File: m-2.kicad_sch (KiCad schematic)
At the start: 26 parts, among them J2 1-2199230-6, M3 M2_2280, Y1 ECS-327MVATX-2-CN-TR3

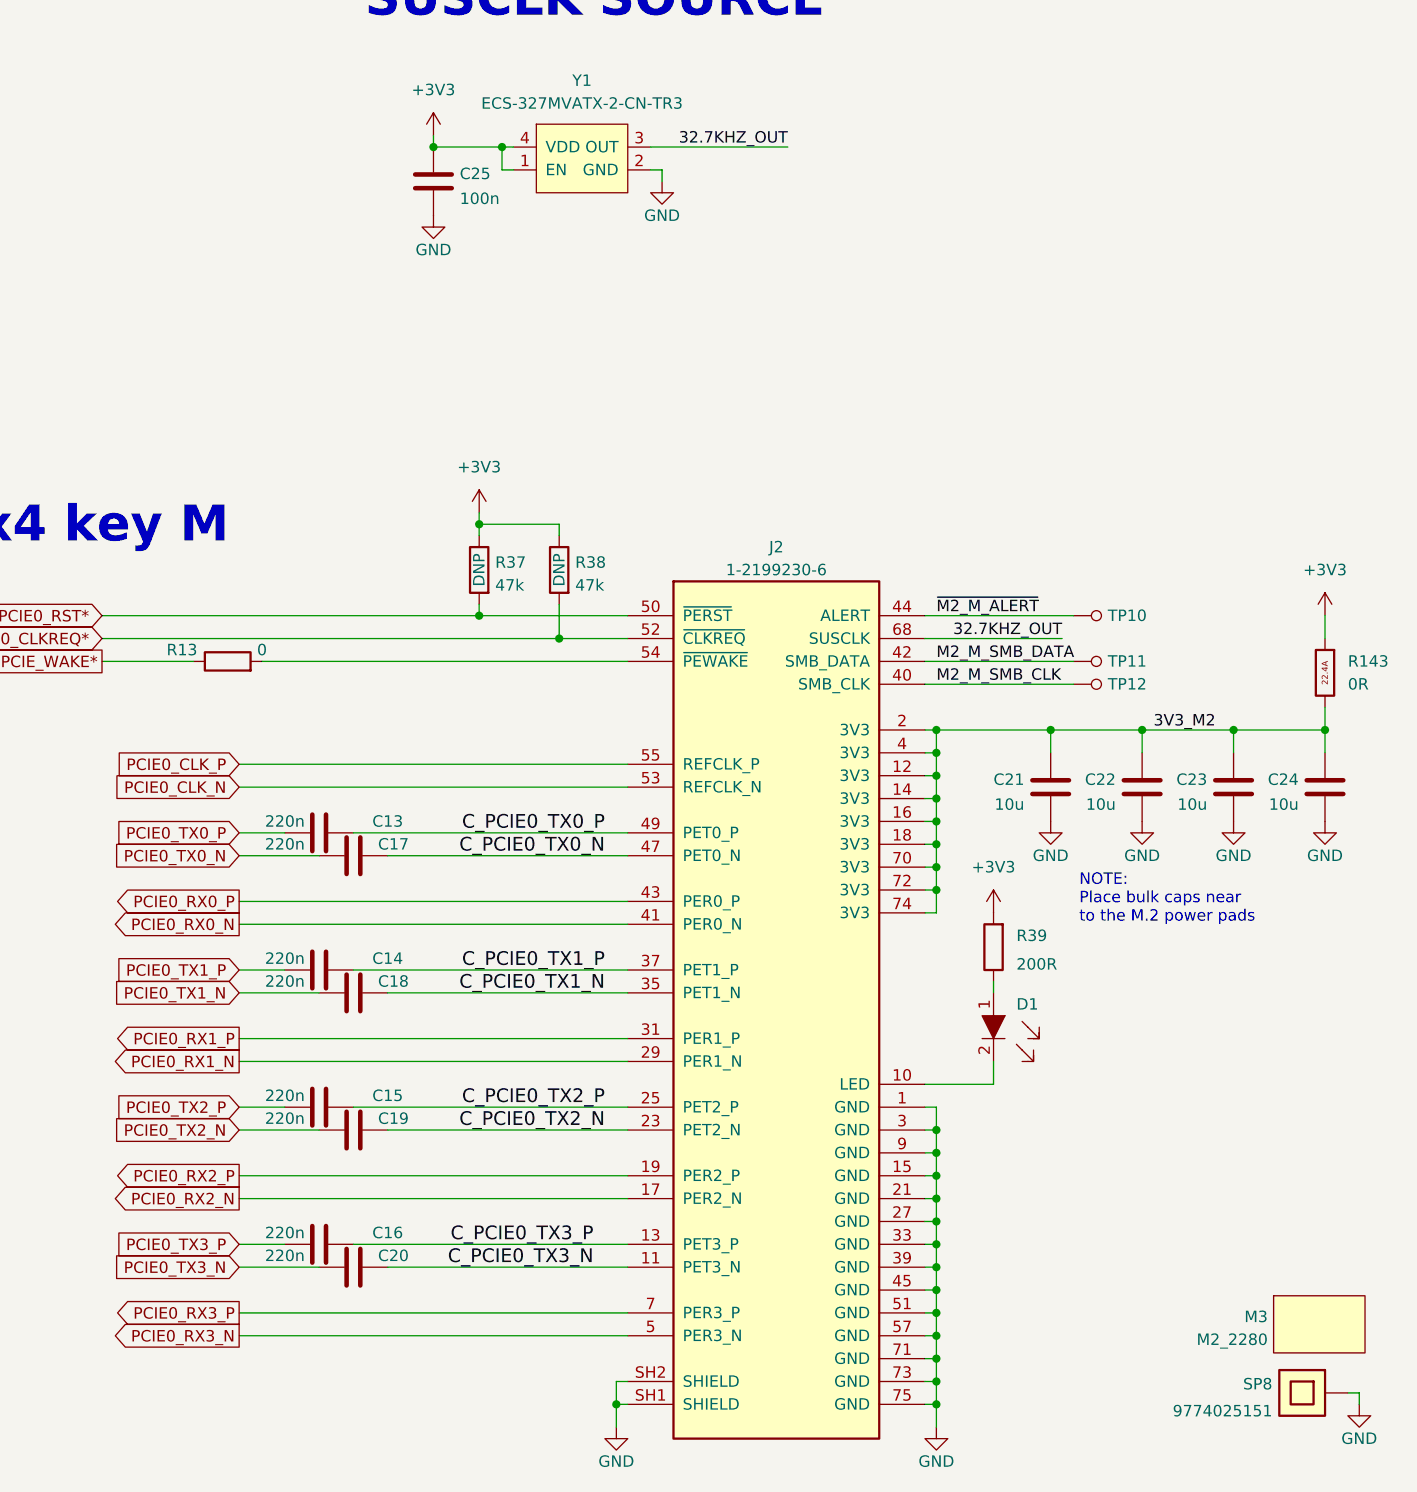
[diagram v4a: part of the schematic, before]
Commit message: Schematic V1 and footprints assigned
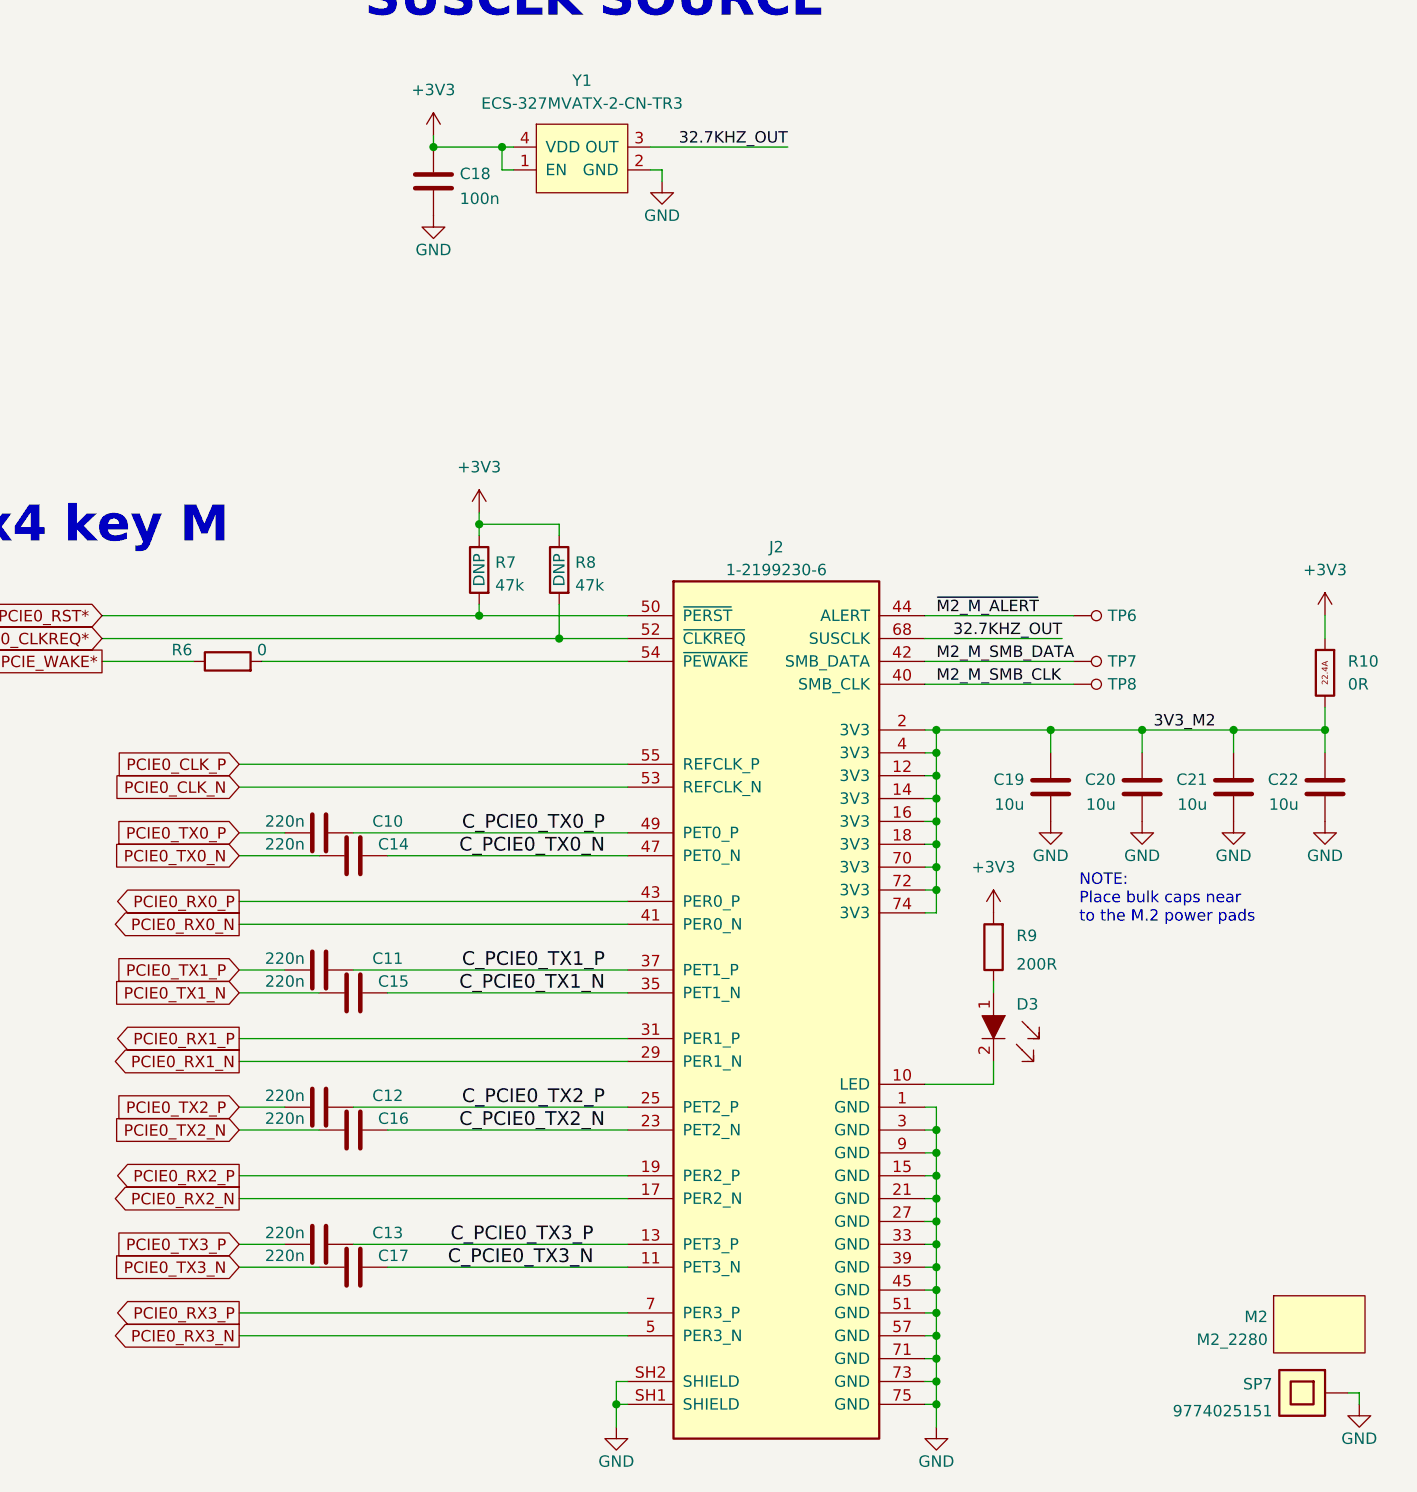
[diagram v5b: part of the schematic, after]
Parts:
- R6: renamed from R13; footprint (none) -> jetson-orin-baseboard-footprints:0402-res
- renumbered C13 to C10, C14 to C11, C15 to C12, C16 to C13, C17 to C14, C18 to C15, C19 to C16, C20 to C17, C25 to C18, C21 to C19, C22 to C20, C23 to C21, C24 to C22, D1 to D3, M3 to M2, R143 to R10, R37 to R7, R38 to R8, R39 to R9, SP8 to SP7, TP10 to TP6, TP11 to TP7, TP12 to TP8
